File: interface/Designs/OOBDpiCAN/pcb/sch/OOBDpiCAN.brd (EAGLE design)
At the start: 65.1 x 57.3 mm, 148 parts, among them IC1 STM32F042CT, IC10 MCP2551SO8, IC11 EEPROM24, IC12 DS3231, IC2 STM32F042CT, IC3 MCP2551SO8, IC4 MCP2551SO8, IC5 ADM3053M, IC6 ADM3053M, IC7 STM32F042CT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

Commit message: add OOBDpiCAN connector
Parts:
- C17, C18: value 10n -> 10u
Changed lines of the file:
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@@
 <element name="JP10" library="SparkFun" package="SJ_2S-NO" value="" x="6.35" y="59.69"/>
 <element name="IC5" library="ADM3053" package="SO20W" value="ADM3053M" x="10.795" y="17.78" rot="R180"/>
-<element name="C17" library="rcl" package="C0603K" value="10n" x="9.8425" y="26.035" rot="R180"/>
+<element name="C17" library="rcl" package="C0603K" value="10u" x="9.8425" y="26.035" rot="R180"/>
 <element name="C19" library="rcl" package="C0603K" value="100n" x="9.8425" y="27.94" rot="R180"/>
 <element name="C15" library="rcl" package="C0805K" value="10u" x="6.35" y="27.94" rot="R180"/>
@@
 <element name="C25" library="rcl" package="C0805K" value="100n" x="5.715" y="9.2075" rot="R180"/>
 <element name="IC6" library="ADM3053" package="SO20W" value="ADM3053M" x="29.845" y="17.78" rot="R180"/>
-<element name="C18" library="rcl" package="C0603K" value="10n" x="28.8925" y="26.035" rot="R180"/>
+<element name="C18" library="rcl" package="C0603K" value="10u" x="28.8925" y="26.035" rot="R180"/>
 <element name="C20" library="rcl" package="C0603K" value="100n" x="28.8925" y="27.94" rot="R180"/>
 <element name="C16" library="rcl" package="C0805K" value="10u" x="25.4" y="27.94" rot="R180"/>

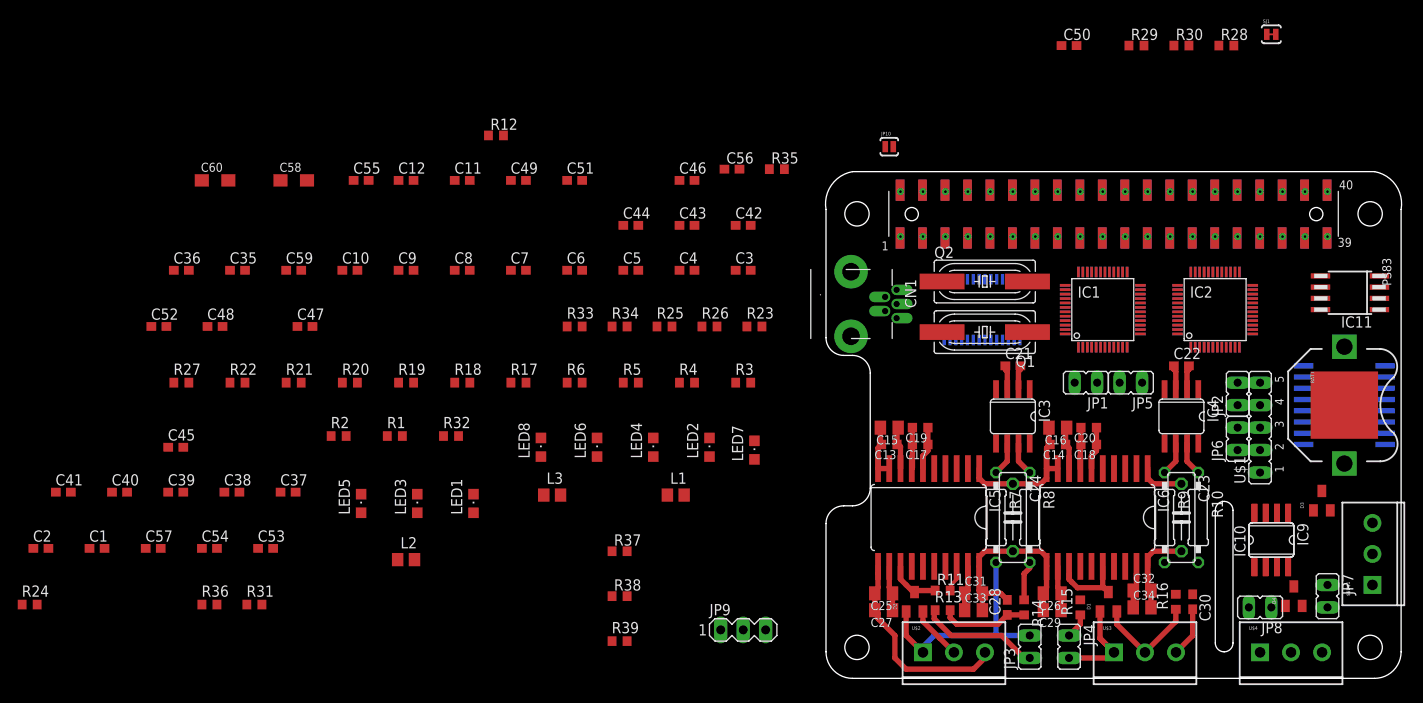
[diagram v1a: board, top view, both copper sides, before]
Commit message: modification on component placing for OOBDpiCAN
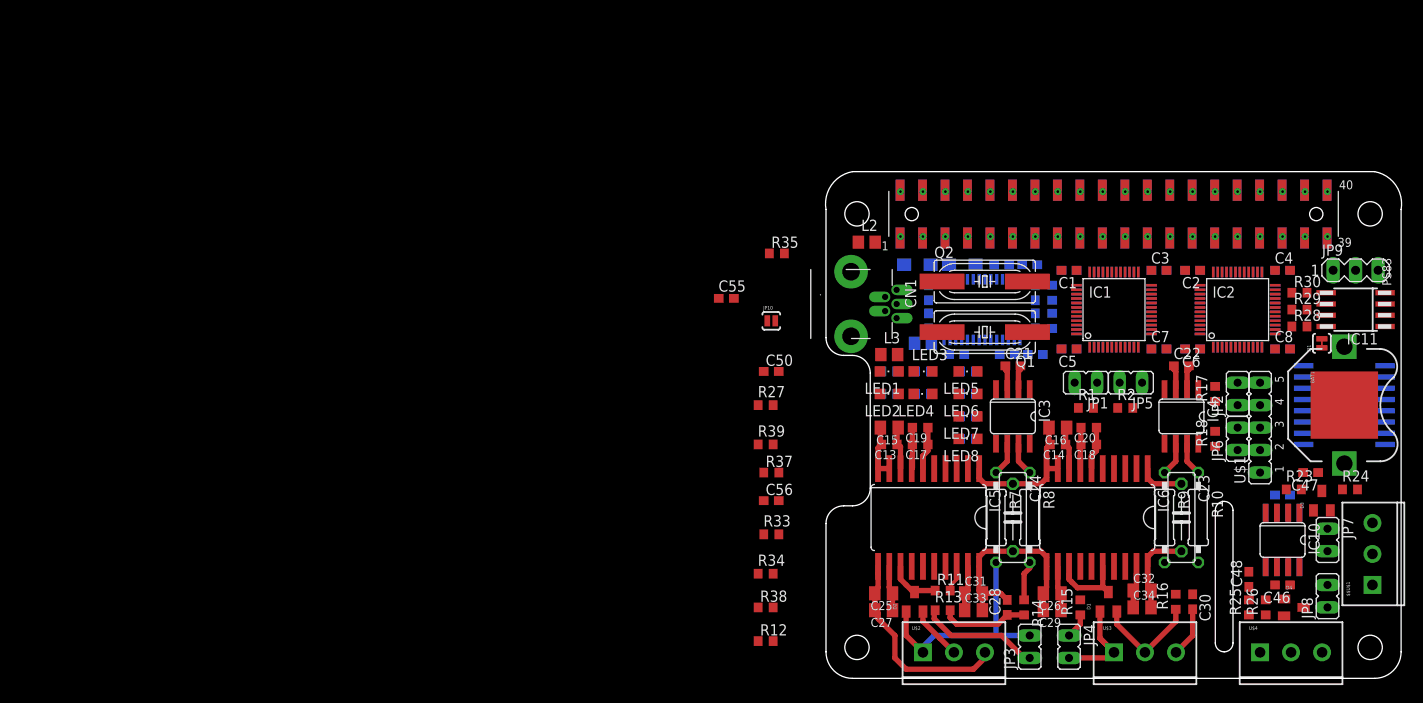
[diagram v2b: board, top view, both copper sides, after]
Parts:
- removed C10, C43, C44, C9: 100nF, resistor:C0603
- moved R24 149.8 mm to (58.4, 21.0)
- moved C2 133.9 mm to (40.6, 45.7), turned to 180 degrees
- moved C41 128.7 mm to (40.6, 36.8), flipped to the bottom
- moved C39 126.1 mm to (50.8, 36.8), flipped to the bottom
- moved C45 125.2 mm to (50.8, 20.3), flipped to the bottom
- moved C48 120.3 mm to (47.0, 10.8), turned to 90 degrees
- moved C40 118.6 mm to (36.8, 36.8), flipped to the bottom
- moved C35 118.1 mm to (50.8, 45.7), flipped to the bottom
- moved C47 114.9 mm to (54.0, 22.9), turned to 180 degrees
- moved C1 114.3 mm to (26.7, 45.7), turned to 180 degrees
- moved C36 110.5 mm to (36.8, 45.7), flipped to the bottom
- moved C37 105.3 mm to (40.6, 45.7), flipped to the bottom
- moved C57 104.1 mm to (22.2, 46.4), flipped to the bottom, turned to 180 degrees
- moved C38 97.9 mm to (26.7, 45.7), flipped to the bottom
- moved R31 96.8 mm to (24.8, 43.2), flipped to the bottom, turned to 270 degrees
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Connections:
- removed net SWCLK1: IC8.37
- removed net SWDIO1: IC8.34
- net +3V3: no longer C10.1, C43.1, C44.1, C9.1
- net GND: no longer C10.2, C43.2, C44.2, C9.2
- net SWCLK: now also IC8.37
- net SWDIO: now also IC8.34

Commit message: finalize first component placement
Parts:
- moved R35 72.2 mm to (61.0, 21.6), flipped to the bottom, turned to 270 degrees
- moved JP10 71.9 mm to (62.9, 22.9), flipped to the bottom, turned to 180 degrees
- moved C50 69.5 mm to (61.0, 48.9), turned to 180 degrees
- moved C56 61.0 mm to (54.0, 22.9), flipped to the bottom, turned to 180 degrees
- moved R38 57.3 mm to (38.7, 41.3)
- moved R37 50.0 mm to (38.7, 43.2)
- moved R39 48.2 mm to (38.7, 39.4)
- moved R12 47.5 mm to (39.4, 10.8), turned to 180 degrees
- moved R34 29.5 mm to (6.35, 37.5), flipped to the bottom
- moved R27 27.4 mm to (19.7, 33.0), flipped to the bottom
- moved R33 23.3 mm to (6.35, 34.9), flipped to the bottom
- moved C55 18.1 mm to (5.71, 45.7), flipped to the bottom, turned to 90 degrees
- moved R22 1.27 mm to (15.2, 25.4)
- moved R20 1.27 mm to (15.2, 30.5)
- moved R21 1.27 mm to (15.2, 27.9)
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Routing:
- net GND: track 42.5 -> 554.5 mm, vias 0 -> 7
- net +5V: track 15.2 -> 267.8 mm, vias 0 -> 12
- net +3V3: track 9.72 -> 236.7 mm, vias 0 -> 1
- net SWCLK: track 0.00 -> 80.3 mm, vias 0 -> 3
- net GNDA: track 76.8 -> 136.4 mm
- net CAN0_TXD: track 0.00 -> 53.4 mm, vias 0 -> 5
- net N$33: track 0.00 -> 51.3 mm
- net CAN2-H: track 0.00 -> 44.7 mm, vias 0 -> 2
- net BOOT0: track 0.00 -> 36.2 mm, vias 0 -> 1
- net CAN2-L: track 0.00 -> 30.1 mm, vias 0 -> 1
- net CAN3-H: track 0.00 -> 29.9 mm, vias 0 -> 2
- net CAN0-H: track 10.6 -> 39.6 mm
- net N$39: track 0.00 -> 28.4 mm
- net N$49: track 0.00 -> 28.3 mm
- net CAN3-L: track 0.00 -> 26.8 mm, vias 0 -> 2
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
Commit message: add initial version of OOBDpiZero rearrange Eagle library files
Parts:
- removed C11, C12: 18pF, resistor:C0603
- removed C17, C18: 10u, rcl:C0603K
- removed Q1: 16MHz, crystal:SM49
- removed R38: 0R, rcl:R0603
- removed R39: 0R, resistor:R0603
- added C10, C9: 10n, rcl:C0603K
- R37: device rcl:R0603 -> rcl:0207/10
- moved R37 33.8 mm to (16.5, 17.8), turned to 90 degrees
- moved R7 0.64 mm to (19.1, 17.8)
- moved CN1 0.32 mm to (-2.54, 42.2)
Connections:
- removed net MC0_1: IC7.5, R38.1
- removed net MCO_0: R37.1
- removed net MCO_1: IC2.5
- removed net MCO_2: IC8.5, R39.2
- removed net N$10: C12.1, IC1.6, Q1.2
- removed net N$11: C11.1, IC1.5, Q1.1
- removed net N$43: IC1.29, R37.2
- removed net N$45: IC2.29, R38.2
- removed net N$46: IC7.29, R39.1
- net +3V3: now also C10.1, C9.1; no longer C17.1, C18.1
- net GND: now also C10.2, C9.2, R37.2; no longer C11.2, C12.2, C17.2, C18.2
- net GNDA: now also R37.1
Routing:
- net SWDIO: track 0.00 -> 58.0 mm, vias 0 -> 2
- net +3V3: track 236.7 -> 288.2 mm, vias 1 -> 7
- net BOOT0: track 36.2 -> 83.9 mm
- net N$29: track 0.00 -> 46.6 mm, vias 0 -> 2
- net N$30: track 0.00 -> 43.0 mm, vias 0 -> 2
- net GND: track 554.5 -> 511.7 mm, vias 7 -> 10
- net N$57: track 0.00 -> 38.0 mm
- net USB2_DM: track 0.00 -> 37.0 mm, vias 0 -> 2
- net USB2_DP: track 0.00 -> 36.6 mm, vias 0 -> 2
- net +5V: track 267.8 -> 231.4 mm, vias 12 -> 16
- net N$56: track 0.00 -> 35.5 mm, vias 0 -> 2
- net N$22: track 0.00 -> 34.0 mm
- net USB1_DM: track 0.00 -> 33.1 mm, vias 0 -> 2
- net N$23: track 0.00 -> 32.4 mm, vias 0 -> 2
- net SWCLK: track 80.3 -> 48.3 mm
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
